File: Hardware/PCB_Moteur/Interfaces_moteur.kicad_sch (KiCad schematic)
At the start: 54 parts, among them J10 Conn_01x02, J11 Conn_01x02, J12 Conn_01x02, J13 Conn_01x02, J14 Conn_01x02, J15 Conn_01x02, J16 Conn_01x06_Pin, J3 Conn_01x03_Socket, J4 Conn_01x03_Socket, J5 Conn_01x03_Socket, J6 Conn_01x03_Socket, J7 Conn_01x02, J8 Conn_01x02, J9 Conn_01x02, U3 MCP1802T-5002I/OT, U4 LSF0204PWR, U5 ISOW1044

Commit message: wip: layout circuits Pyro
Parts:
- R18: footprint Resistor_SMD:R_0603_1608Metric -> Resistor_SMD:R_0805_2012Metric
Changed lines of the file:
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@@
 			)
 		)
-		(property "Footprint" "Resistor_SMD:R_0603_1608Metric"
+		(property "Footprint" "Resistor_SMD:R_0805_2012Metric"
 			(at 121.92 71.628 90)
 			(effects

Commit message: wip: fin des circuits sauf ceux du STM
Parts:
- J3, J4, J5, J6: footprint Connector_PinHeader_1.00mm:PinHeader_1x03_P1.00mm_Vertical -> Connector_PinHeader_2.54mm:PinHeader_1x03_P2.54mm_Vertical
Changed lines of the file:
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@@
 			)
 		)
-		(property "Footprint" "Connector_PinHeader_1.00mm:PinHeader_1x03_P1.00mm_Vertical"
+		(property "Footprint" "Connector_PinHeader_2.54mm:PinHeader_1x03_P2.54mm_Vertical"
 			(at 78.74 125.73 0)
 			(effects
@@
 			)
 		)
-		(property "Footprint" "Connector_PinHeader_1.00mm:PinHeader_1x03_P1.00mm_Vertical"
+		(property "Footprint" "Connector_PinHeader_2.54mm:PinHeader_1x03_P2.54mm_Vertical"
 			(at 109.22 125.73 0)
 			(effects
@@
 			)
 		)
-		(property "Footprint" "Connector_PinHeader_1.00mm:PinHeader_1x03_P1.00mm_Vertical"
+		(property "Footprint" "Connector_PinHeader_2.54mm:PinHeader_1x03_P2.54mm_Vertical"
 			(at 139.7 125.73 0)
 			(effects
@@
 			)
 		)
-		(property "Footprint" "Connector_PinHeader_1.00mm:PinHeader_1x03_P1.00mm_Vertical"
+		(property "Footprint" "Connector_PinHeader_2.54mm:PinHeader_1x03_P2.54mm_Vertical"
 			(at 46.99 125.73 0)
 			(effects

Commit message: wip: layout presque fini (decoup stm32 restant)
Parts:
- C32, C36: footprint Capacitor_SMD:C_0805_2012Metric -> Capacitor_SMD:C_0603_1608Metric
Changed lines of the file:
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@@
 			)
 		)
-		(property "Footprint" "Capacitor_SMD:C_0805_2012Metric"
+		(property "Footprint" "Capacitor_SMD:C_0603_1608Metric"
 			(at 268.9352 53.34 0)
 			(effects
@@
 			)
 		)
-		(property "Footprint" "Capacitor_SMD:C_0805_2012Metric"
+		(property "Footprint" "Capacitor_SMD:C_0603_1608Metric"
 			(at 194.0052 57.15 0)
 			(effects

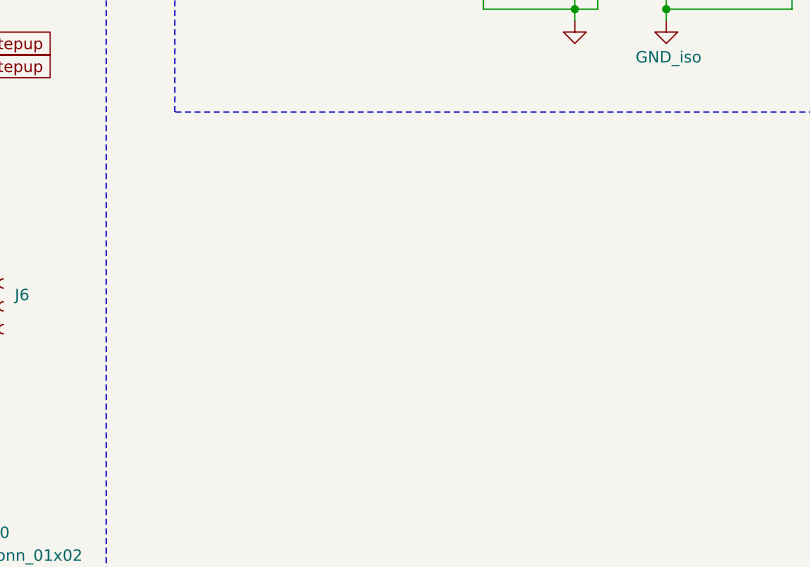
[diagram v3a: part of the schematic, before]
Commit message: wip: nouveaux connecteurs et espace pour ceux-ci
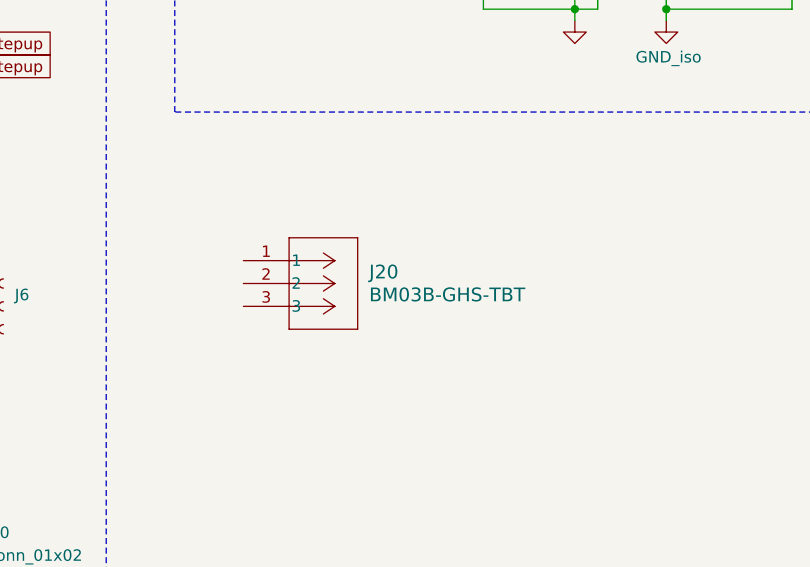
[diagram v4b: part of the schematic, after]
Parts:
- added J20: BM03B-GHS-TBT, pcb_moteur:CONN_BM03B-GHS-TBT_JST, symbol pcb_moteur:BM03B-GHS-TBT
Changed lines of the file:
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@@
+	)
+	(symbol
+		(lib_id "pcb_moteur:BM03B-GHS-TBT")
+		(at 166.37 120.65 0)
+		(unit 1)
+		(exclude_from_sim no)
+		(in_bom yes)
+		(on_board yes)
+		(dnp no)
+		(fields_autoplaced yes)
+		(property "Reference" "J20"
+			(at 180.34 121.9199 0)
+			(effects
+				(font
+					(size 1.524 1.524)
+				)
+				(justify left)
+			)
+		)
+		(property "Value" "BM03B-GHS-TBT"
+			(at 180.34 124.4599 0)
+			(effects
+				(font
+					(size 1.524 1.524)
+				)
+				(justify left)
+			)
+		)
+		(property "Footprint" "pcb_moteur:CONN_BM03B-GHS-TBT_JST"
+			(at 166.37 120.65 0)
+			(effects
+				(font
+					(size 1.27 1.27)
+					(italic yes)
+				)
+				(hide yes)
+			)
+		)
+		(property "Datasheet" "BM03B-GHS-TBT"
+			(at 166.37 120.65 0)
+			(effects
+				(font
+					(size 1.27 1.27)
+					(italic yes)
+				)
+				(hide yes)
+			)
+		)
+		(property "Description" ""
+			(at 166.37 120.65 0)
+			(effects
+				(font
+					(size 1.27 1.27)
+				)
+				(hide yes)
+			)
+		)
+		(pin "1"
+		)
+		(pin "3"
+		)
+		(pin "2"
+		)
+		(instances
+			(project ""
+				(path "/b0d87684-7b1c-41d8-8358-755aa327573e/a8ed0c04-b51e-4eec-84d1-0b2303d57d27"
+					(reference "J20")
+					(unit 1)
+				)
+			)
+		)
 	)
 	(symbol

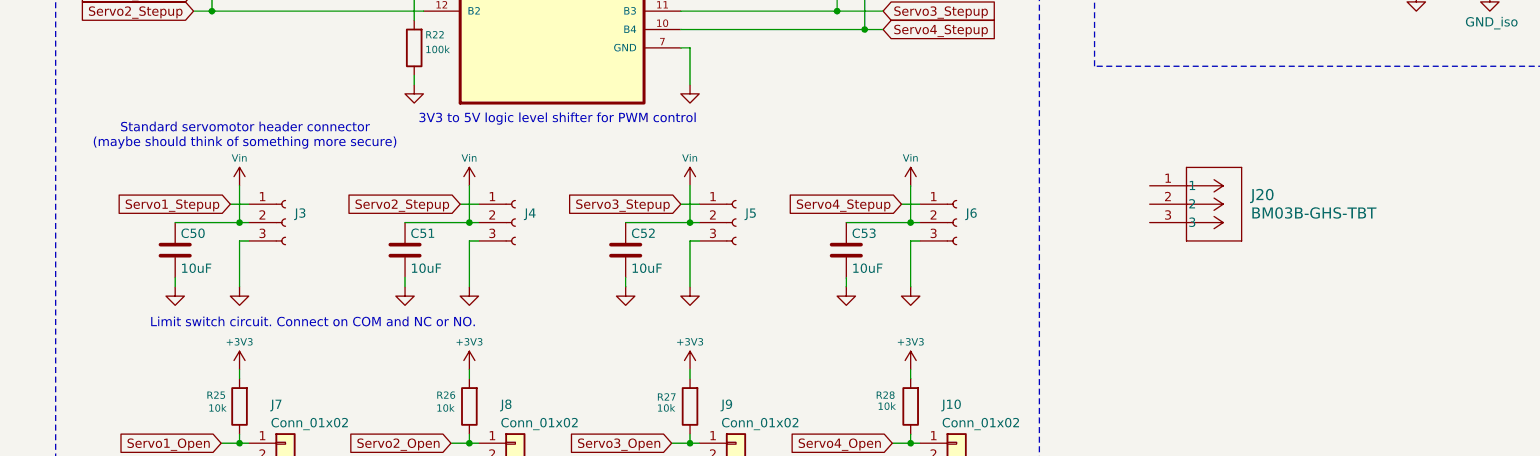
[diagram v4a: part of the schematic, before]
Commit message: wip: arrangement connecteurs et modeles 3D
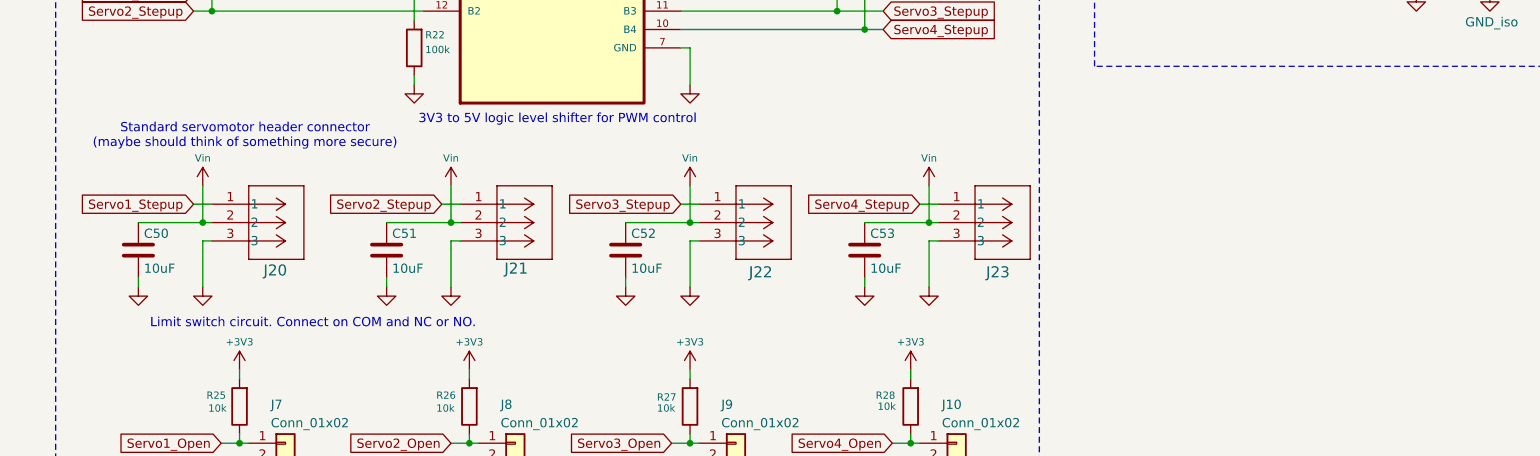
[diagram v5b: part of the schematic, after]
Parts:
- removed J3, J4, J5, J6: Conn_01x03_Socket, Connector_PinHeader_2.54mm:PinHeader_1x03_P2.54mm_Vertical, symbol Connector:Conn_01x03_Socket
- added J21, J22, J23: BM03B-GHS-TBT, pcb_moteur:CONN_BM03B-GHS-TBT_JST, symbol pcb_moteur:BM03B-GHS-TBT
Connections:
- net GND: now also J20.3, J21.3, J22.3, J23.3
- net Servo1_Stepup: now also J20.1
- net Servo2_Stepup: now also J21.1
- net Servo3_Stepup: now also J22.1
- net Servo4_Stepup: now also J23.1
- net Vin: now also J20.2, J21.2, J22.2, J23.2
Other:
- moved on the sheet: C50, C51, C53, J20

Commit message: wip: routing (suite)
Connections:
- net CAN-: now reaches J15.2 (Pin_2), R35.1, U5.18 (CANL)
- net CAN+: now reaches J15.1 (Pin_1), R34.2, U5.19 (CANH)
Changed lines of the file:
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@@
+		)
+	)
+	(label "CAN-"
+		(at 246.38 81.28 0)
+		(effects
+			(font
+				(size 1.27 1.27)
+			)
+			(justify left bottom)
+		)
+	)
+	(label "CAN+"
+		(at 246.38 66.04 0)
+		(effects
+			(font
+				(size 1.27 1.27)
+			)
+			(justify left bottom)
 		)
 	)

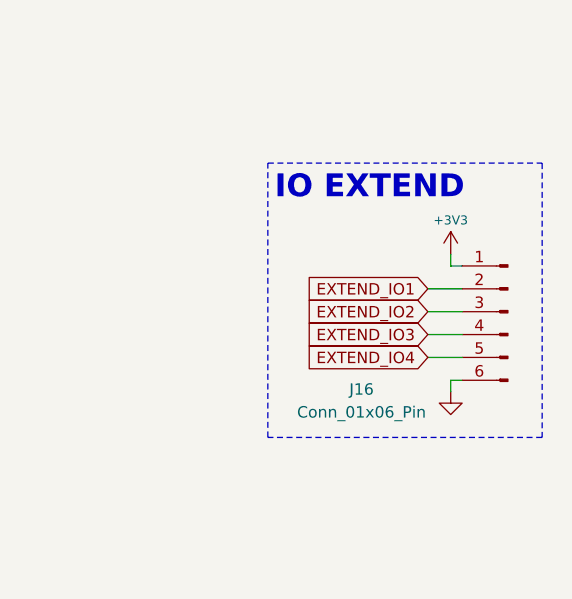
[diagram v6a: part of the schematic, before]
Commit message: feat(moteur): add 8MHz crystal (only schematic), fix ERC, update stm32 project, remove extend ios
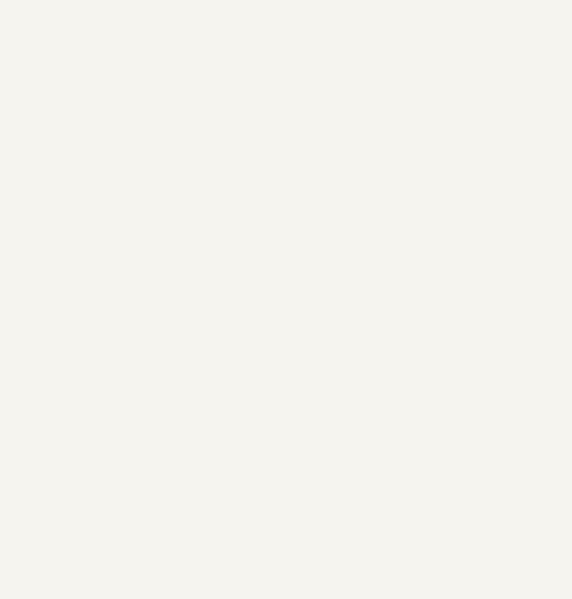
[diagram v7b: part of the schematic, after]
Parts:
- removed J16: Conn_01x06_Pin, Connector_PinSocket_2.54mm:PinSocket_2x03_P2.54mm_Vertical, symbol Connector:Conn_01x06_Pin
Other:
- note removed: "IO EXTEND"

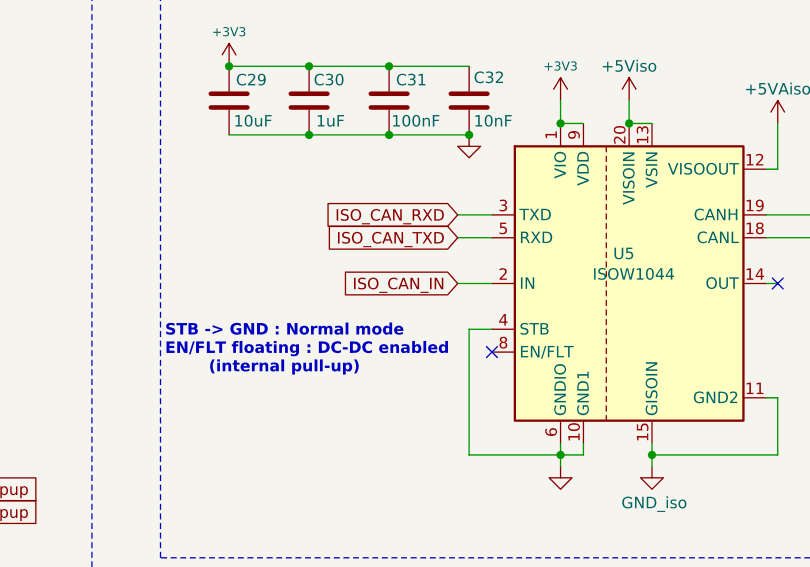
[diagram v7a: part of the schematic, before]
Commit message: fix(gse & moteur): mapping + routing, remove CAN_ISO_IN/OUT
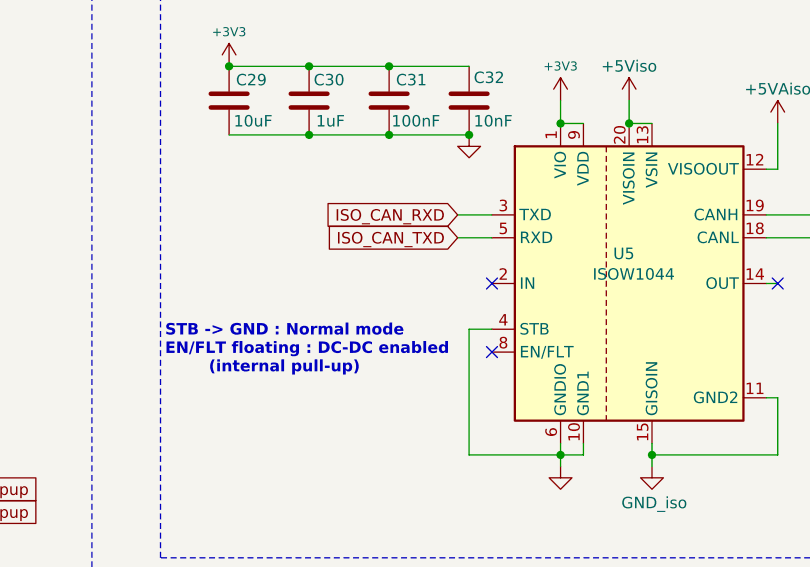
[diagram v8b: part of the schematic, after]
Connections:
- net ISO_CAN_IN: no longer names the net of U5.2 (IN)
- no-connect marks 3 -> 4
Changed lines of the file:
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@@
+	)
+	(no_connect
+		(at 195.58 73.66)
 	)
 	(no_connect
@@
 		(pts
 			(xy 227.33 55.88) (xy 227.33 60.96)
-		)
-		(stroke
-			(width 0)
-			(type default)
-		)
-	)
-	(wire
-		(pts
-			(xy 191.77 73.66) (xy 195.58 73.66)
 		)
 		(stroke
@@
 			(effects
 				(font
-					(size 1.27 1.27)
-				)
-				(justify right)
-				(hide yes)
-			)
-		)
-	)
-	(global_label "ISO_CAN_IN"
-		(shape input)
-		(at 191.77 73.66 180)
-		(fields_autoplaced yes)
-		(effects
-			(font
-				(size 1.27 1.27)
-			)
-			(justify right)
-		)
-		(property "Intersheetrefs" "${INTERSHEET_REFS}"
-			(at 178.0804 73.66 0)
-			(effects
-				(font
